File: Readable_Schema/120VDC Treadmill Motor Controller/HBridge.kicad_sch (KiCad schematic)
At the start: 77 parts, among them J2 OSTT7020150, Q1 IPP60R060P7XKSA1, Q2 IPP60R060P7XKSA1, Q3 IPP60R060P7XKSA1, Q4 IPP60R060P7XKSA1, U1 UCC21530DWKR, U2 UCC21530DWKR

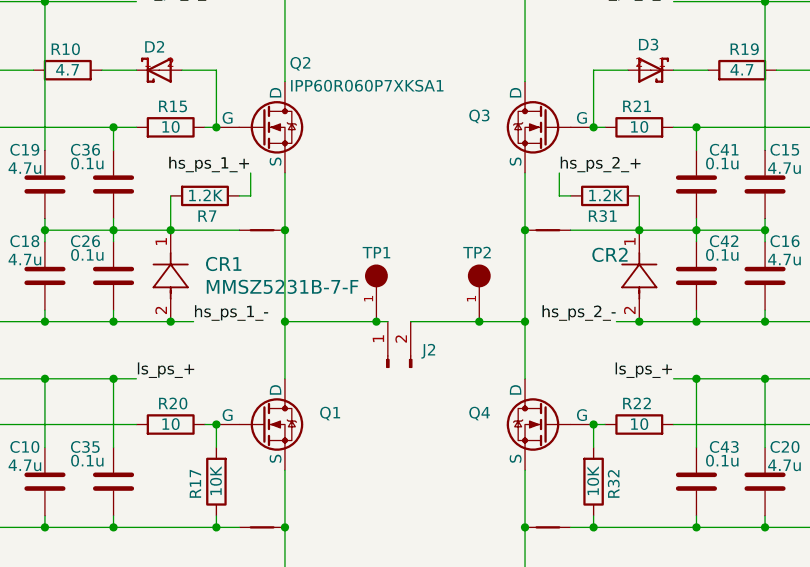
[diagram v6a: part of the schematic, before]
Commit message: -Rotated a few components --Playing with different layout ideas, no major changes
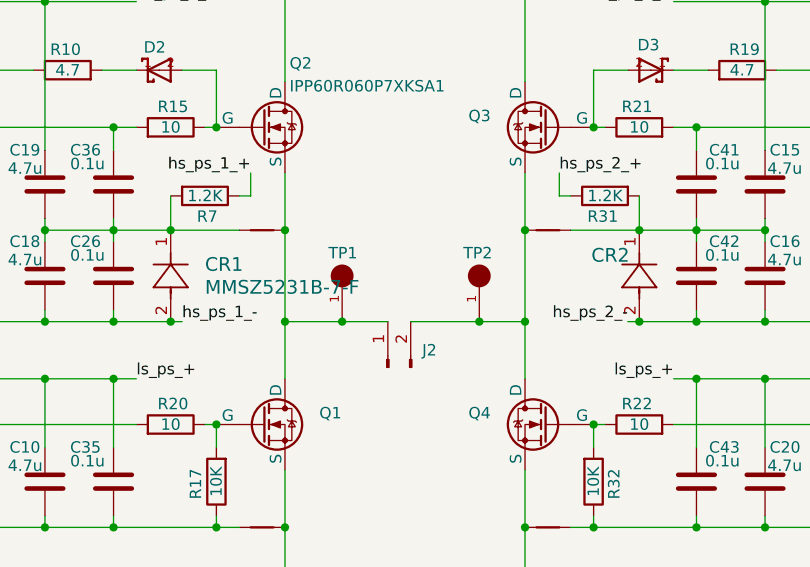
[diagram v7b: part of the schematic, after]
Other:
- moved on the sheet: TP1
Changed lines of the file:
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@@
 	)
 	(junction
-		(at 144.78 110.49)
-		(diameter 0)
-		(color 0 0 0 0)
-	)
-	(junction
 		(at 161.29 49.53)
 		(diameter 0)
@@
 	)
 	(junction
+		(at 140.97 110.49)
+		(diameter 0)
+		(color 0 0 0 0)
+	)
+	(junction
 		(at 173.99 100.33)
 		(diameter 0)
@@
 	(wire
 		(pts
+			(xy 140.97 110.49) (xy 146.05 110.49)
+		)
+		(stroke
+			(width 0)
+			(type default)
+		)
+	)
+	(wire
+		(pts
 			(xy 115.57 132.08) (xy 115.57 133.35)
 		)
@@
 	(wire
 		(pts
-			(xy 134.62 110.49) (xy 144.78 110.49)
+			(xy 134.62 110.49) (xy 140.97 110.49)
 		)
 		(stroke
@@
 	(wire
 		(pts
-			(xy 144.78 110.49) (xy 146.05 110.49)
-		)
-		(stroke
-			(width 0)
-			(type default)
-		)
-	)
-	(wire
-		(pts
 			(xy 193.04 119.38) (xy 199.39 119.38)
 		)
@@
 	(wire
 		(pts
-			(xy 171.45 110.49) (xy 173.99 110.49)
+			(xy 172.72 110.49) (xy 173.99 110.49)
 		)
 		(stroke
@@
 	(wire
 		(pts
-			(xy 121.92 110.49) (xy 124.46 110.49)
+			(xy 121.92 110.49) (xy 123.19 110.49)
 		)
 		(stroke
@@
 	)
 	(label "hs_ps_2_-"
-		(at 171.45 110.49 180)
+		(at 172.72 110.49 180)
 		(effects
 			(font
@@
 	)
 	(label "hs_ps_1_-"
-		(at 124.46 110.49 0)
+		(at 123.19 110.49 0)
 		(effects
 			(font
@@
 	(symbol
 		(lib_id "Treadmill_Comp:RCWCTE")
-		(at 144.78 105.41 90)
+		(at 140.97 105.41 90)
 		(unit 1)
 		(exclude_from_sim no)
@@
 		(dnp no)
 		(property "Reference" "TP1"
-			(at 143.256 102.87 90)
+			(at 139.446 102.87 90)
 			(effects
 				(font
@@
 		)
 		(property "Value" "RCWCTE"
-			(at 147.32 106.6799 90)
+			(at 143.51 106.6799 90)
 			(effects
 				(font
@@
 		)
 		(property "Footprint" "Treadmill_Feet:RCWCTE"
-			(at 144.78 105.41 0)
+			(at 140.97 105.41 0)
 			(effects
 				(font
@@
 		)
 		(property "Datasheet" "https://www.koaspeer.com/pdfs/RC.pdf"
-			(at 144.78 105.41 0)
+			(at 140.97 105.41 0)
 			(effects
 				(font
@@
 		)
 		(property "Description" "https://www.digikey.com/en/products/detail/koa-speer-electronics-inc/RCWCTE/11476558"
-			(at 144.78 105.41 0)
+			(at 140.97 105.41 0)
 			(effects
 				(font
@@
 		)
 		(property "PARTREV" "1/06/14"
-			(at 144.78 105.41 0)
+			(at 140.97 105.41 0)
 			(effects
 				(font
@@
 		)
 		(property "SNAPEDA_PN" "RCWCTE"
-			(at 144.78 105.41 0)
+			(at 140.97 105.41 0)
 			(effects
 				(font
@@
 		)
 		(property "MANUFACTURER" "KOA Speer"
-			(at 144.78 105.41 0)
+			(at 140.97 105.41 0)
 			(effects
 				(font
@@
 		)
 		(property "MAXIMUM_PACKAGE_HEIGHT" "2 mm"
-			(at 144.78 105.41 0)
+			(at 140.97 105.41 0)
 			(effects
 				(font
@@
 		)
 		(property "STANDARD" "Manufacturer Recommendations"
-			(at 144.78 105.41 0)
+			(at 140.97 105.41 0)
 			(effects
 				(font

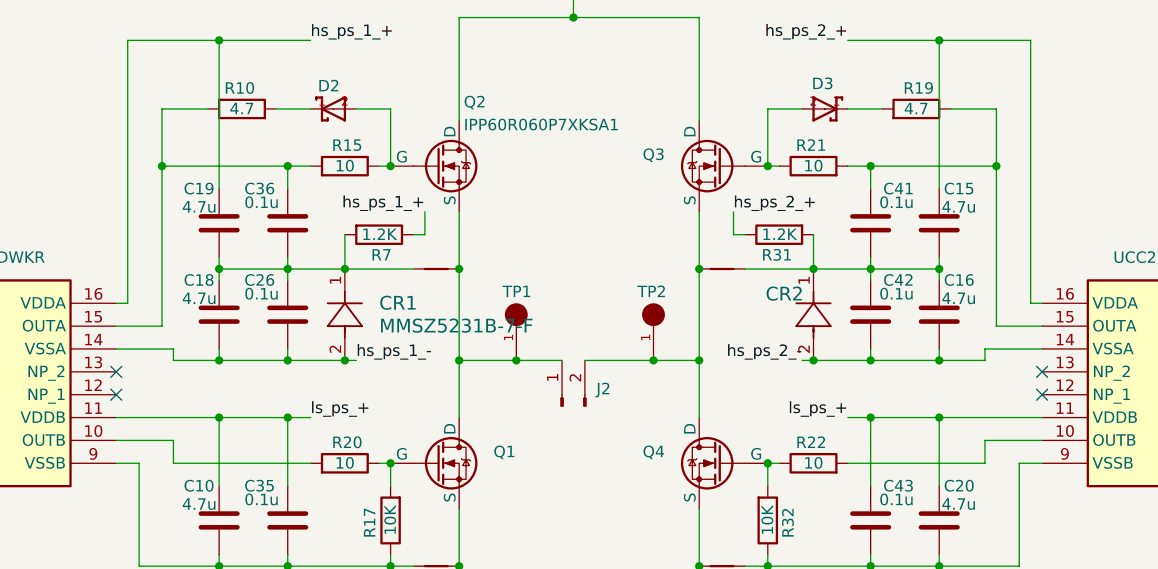
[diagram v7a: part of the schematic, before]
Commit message: -Finally figured out how to use a board fill. Despite having changed number of board layers at home and adding the netclasses, those board settings aren't showing up here --If board settings arent globally updated after this push then we need to do some work to understand the problem.
-Repositioning components to try and get them to share similar pours

-Still need to figure out how to set things up to be able to add solder to the High current lines
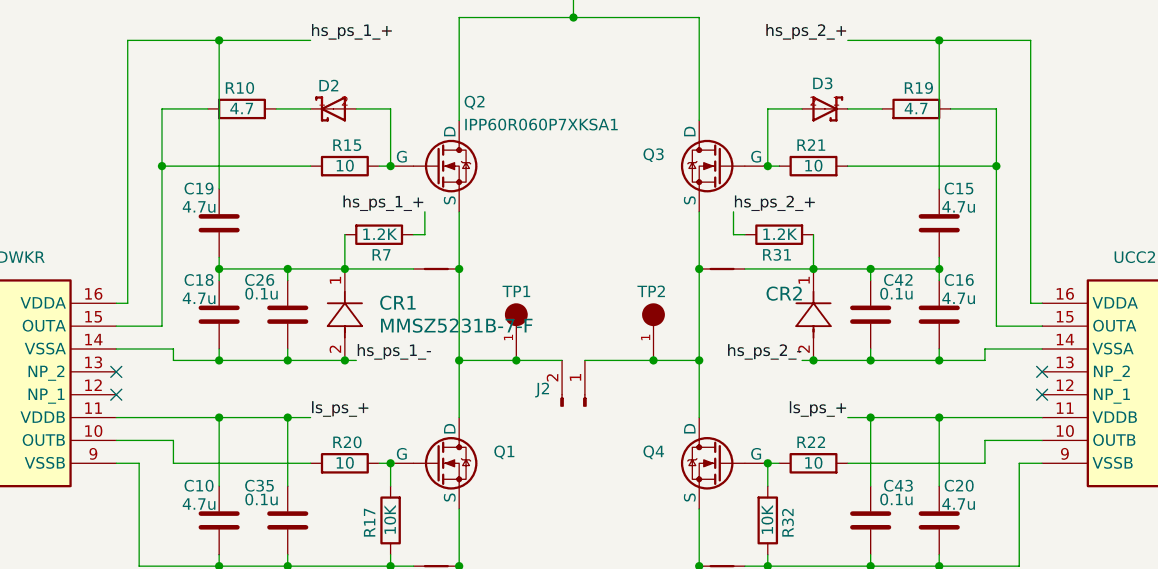
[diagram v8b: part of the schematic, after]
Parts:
- removed C36, C41: 0.1u, Capacitor_SMD:C_0201_0603Metric_Pad0.64x0.40mm_HandSolder, symbol Device:C
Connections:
- net at NT2.1, Q3.3 (S), Q4.2 (D)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: now also J2.1 (Pin_1); no longer J2.2 (Pin_2)
- net at NT1.2, Q1.2 (D), Q2.3 (S)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: now also J2.2 (Pin_2); no longer J2.1 (Pin_1)
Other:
- moved on the sheet: J2
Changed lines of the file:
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@@
 	)
 	(junction
-		(at 180.34 88.9)
-		(diameter 0)
-		(color 0 0 0 0)
-	)
-	(junction
 		(at 140.97 110.49)
 		(diameter 0)
@@
 	)
 	(junction
-		(at 115.57 88.9)
-		(diameter 0)
-		(color 0 0 0 0)
-	)
-	(junction
 		(at 241.3 139.7)
 		(diameter 0)
@@
 	(wire
 		(pts
-			(xy 194.31 88.9) (xy 180.34 88.9)
+			(xy 177.8 88.9) (xy 194.31 88.9)
 		)
 		(stroke
@@
 	(wire
 		(pts
-			(xy 115.57 88.9) (xy 118.11 88.9)
+			(xy 101.6 88.9) (xy 118.11 88.9)
 		)
 		(stroke
@@
 	(wire
 		(pts
-			(xy 101.6 88.9) (xy 115.57 88.9)
-		)
-		(stroke
-			(width 0)
-			(type default)
-		)
-	)
-	(wire
-		(pts
 			(xy 247.65 101.6) (xy 233.68 101.6)
 		)
@@
 	(wire
 		(pts
-			(xy 115.57 99.06) (xy 115.57 100.33)
-		)
-		(stroke
-			(width 0)
-			(type default)
-		)
-	)
-	(wire
-		(pts
 			(xy 229.87 116.84) (xy 233.68 116.84)
 		)
@@
 	(wire
 		(pts
-			(xy 115.57 88.9) (xy 115.57 91.44)
-		)
-		(stroke
-			(width 0)
-			(type default)
-		)
-	)
-	(wire
-		(pts
 			(xy 127 133.35) (xy 129.54 133.35)
 		)
@@
 	(wire
 		(pts
-			(xy 180.34 99.06) (xy 180.34 100.33)
-		)
-		(stroke
-			(width 0)
-			(type default)
-		)
-	)
-	(wire
-		(pts
 			(xy 146.05 146.05) (xy 146.05 140.97)
 		)
@@
 	(wire
 		(pts
-			(xy 180.34 88.9) (xy 177.8 88.9)
-		)
-		(stroke
-			(width 0)
-			(type default)
-		)
-	)
-	(wire
-		(pts
 			(xy 62.23 106.68) (xy 62.23 101.6)
 		)
@@
 	(wire
 		(pts
-			(xy 180.34 88.9) (xy 180.34 91.44)
-		)
-		(stroke
-			(width 0)
-			(type default)
-		)
-	)
-	(wire
-		(pts
 			(xy 168.91 133.35) (xy 166.37 133.35)
 		)
@@
 		(length 2.54)
 		(shape round)
+		(at 140.97 140.97 0)
+		(fields_autoplaced yes)
+		(effects
+			(font
+				(size 1.27 1.27)
+			)
+			(justify left bottom)
+		)
+		(property "Netclass" "HIGH CURRENT"
+			(at 141.6685 138.43 0)
+			(effects
+				(font
+					(size 1.27 1.27)
+				)
+				(justify left)
+				(hide yes)
+			)
+		)
+		(property "Component Class" ""
+			(at -39.37 60.96 0)
+			(effects
+				(font
+					(size 1.27 1.27)
+					(italic yes)
+				)
+			)
+		)
+	)
+	(netclass_flag ""
+		(length 2.54)
+		(shape round)
 		(at 53.34 21.59 0)
 		(effects
@@
 	)
 	(symbol
-		(lib_id "Device:C")
-		(at 180.34 95.25 0)
-		(mirror y)
-		(unit 1)
-		(exclude_from_sim no)
-		(in_bom yes)
-		(on_board yes)
-		(dnp no)
-		(property "Reference" "C41"
-			(at 185.166 91.44 0)
-			(effects
-				(font
-					(size 1.27 1.27)
-				)
-				(justify left)
-			)
-		)
-		(property "Value" "0.1u"
-			(at 185.166 92.964 0)
-			(effects
-				(font
-					(size 1.27 1.27)
-				)
-				(justify left)
-			)
-		)
-		(property "Footprint" "Capacitor_SMD:C_0201_0603Metric_Pad0.64x0.40mm_HandSolder"
-			(at 179.3748 99.06 0)
-			(effects
-				(font
-					(size 1.27 1.27)
-				)
-				(hide yes)
-			)
-		)
-		(property "Datasheet" "https://mm.digikey.com/Volume0/opasdata/d220001/medias/docus/729/CL05B104KA5NNNC_Spec.pdf"
-			(at 180.34 95.25 0)
-			(effects
-				(font
-					(size 1.27 1.27)
-				)
-				(hide yes)
-			)
-		)
-		(property "Description" "CL05B104KA5NNNC"
-			(at 180.34 95.25 0)
-			(effects
-				(font
-					(size 1.27 1.27)
-				)
-				(hide yes)
-			)
-		)
-		(pin "1"
-		)
-		(pin "2"
-		)
-		(instances
-			(project "120VDC Treadmill Motor Controller"
-				(path "/319bc5c0-2dd5-4df3-a34b-9170833ebccd/49a5a11b-8174-445d-b343-1fe5ec8c60de"
-					(reference "C41")
-					(unit 1)
-				)
-			)
-		)
-	)
-	(symbol
 		(lib_id "Device:R")
 		(at 29.21 45.72 90)
@@
 	(symbol
 		(lib_id "Connector:Conn_01x02_Pin")
-		(at 146.05 115.57 90)
+		(at 148.59 115.57 270)
+		(mirror x)
 		(unit 1)
 		(exclude_from_sim no)
@@
 		(dnp no)
 		(property "Reference" "J2"
-			(at 149.86 113.6649 90)
+			(at 144.78 113.6649 90)
 			(effects
 				(font
@@
 		)
 		(property "Value" "OSTT7020150"
-			(at 144.78 116.2049 90)
+			(at 149.86 116.2049 90)
 			(effects
 				(font
@@
 		)
 		(property "Footprint" "Treadmill_Feet:CONN2_OSTT7020150_OST"
-			(at 146.05 115.57 0)
+			(at 148.59 115.57 0)
 			(effects
 				(font
@@
 		)
 		(property "Datasheet" "https://mm.digikey.com/Volume0/opasdata/d220001/medias/docus/388/OSTT7xx0150.pdf"
-			(at 146.05 115.57 0)
+			(at 148.59 115.57 0)
 			(effects
 				(font
@@
 		)
 		(property "Description" "OSTT7020150"
-			(at 146.05 115.57 0)
+			(at 148.59 115.57 0)
 			(effects
 				(font
@@
 		)
 		(instances
-			(project ""
+			(project "120VDC Treadmill Motor Controller"
 				(path "/319bc5c0-2dd5-4df3-a34b-9170833ebccd/49a5a11b-8174-445d-b343-1fe5ec8c60de"
 					(reference "J2")
@@
 					(unit 1)
 				)
-			)
-		)
-	)
-	(symbol
-		(lib_id "Device:C")
-		(at 115.57 95.25 0)
-		(unit 1)
-		(exclude_from_sim no)
-		(in_bom yes)
-		(on_board yes)
-		(dnp no)
-		(property "Reference" "C36"
-			(at 110.744 91.44 0)
-			(effects
-				(font
-					(size 1.27 1.27)
-				)
-				(justify left)
-			)
-		)
-		(property "Value" "0.1u"
-			(at 110.744 92.964 0)
-			(effects
-				(font
-					(size 1.27 1.27)
-				)
-				(justify left)
-			)
-		)
-		(property "Footprint" "Capacitor_SMD:C_0201_0603Metric_Pad0.64x0.40mm_HandSolder"
-			(at 116.5352 99.06 0)
-			(effects
-				(font
-					(size 1.27 1.27)
-				)
-				(hide yes)
-			)
-		)
-		(property "Datasheet" "https://mm.digikey.com/Volume0/opasdata/d220001/medias/docus/729/CL05B104KA5NNNC_Spec.pdf"
-			(at 115.57 95.25 0)
-			(effects
-				(font
-					(size 1.27 1.27)
-				)
-				(hide yes)
-			)
-		)
-		(property "Description" "CL05B104KA5NNNC"
-			(at 115.57 95.25 0)
-			(effects
-				(font
-					(size 1.27 1.27)
-				)
-				(hide yes)
-			)
-		)
-		(pin "1"
-		)
-		(pin "2"
-		)
-		(instances
-			(project "120VDC Treadmill Motor Controller"
-				(path "/319bc5c0-2dd5-4df3-a34b-9170833ebccd/49a5a11b-8174-445d-b343-1fe5ec8c60de"
-					(reference "C36")
-					(unit 1)
-				)
